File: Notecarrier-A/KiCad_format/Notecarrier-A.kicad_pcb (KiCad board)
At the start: 2 copper layers, 0 parts

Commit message: Establish port of Notecarrier-B PCB.
Ported: components, board outline, fabrication layers, silkscreens and front copper.
To go: inner and back copper layers, drills, sheet metadata.
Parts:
- added ANT1: NN03-310, blues-kicad-lib:ANT-NN03310-LTE_NO-SILK, F.Cu at (79.0, 74.5)
- added ANT2: NN03-320, blues-kicad-lib:ANT-NN03320-GPS_NO-SILK, F.Cu at (59.0, 100.5)
- added BAT1: NU, blues-kicad-lib:BATHLD-2464-NO_MECH, B.Cu at (92.5, 112.8)
- added C1: 47u/16V-X5R, blues-kicad-lib:CS-C-1206, F.Cu at (74.9, 119.5)
- added C10: 100n/16V, blues-kicad-lib:CS-C-0402, F.Cu at (70.7, 116.9)
- added C11: 10n/1kV, blues-kicad-lib:CS-C-1206, F.Cu at (63.1, 119.4)
- added C12: 10u/25V-X5R, blues-kicad-lib:CS-C-1206, F.Cu at (119.0, 129.7)
- added C13: 1u/16V-X5R, blues-kicad-lib:CS-C-0402, F.Cu at (115.5, 116.8)
- added C16: 100n/16V, blues-kicad-lib:CS-C-0402, F.Cu at (110.9, 90.8)
- added C17: 33p/50V-C0G, blues-kicad-lib:CS-C-0402, F.Cu at (113.4, 90.8)
- added C18: 33p/50V-C0G, blues-kicad-lib:CS-C-0402, F.Cu at (111.6, 95.6)
- added C19: 33p/50V-C0G, blues-kicad-lib:CS-C-0402, F.Cu at (113.5, 93.5)
- added C2: 4.7u/6.3V-X5R, blues-kicad-lib:CS-C-0402, F.Cu at (76.5, 120.7)
- added C21: 1n/50V, blues-kicad-lib:FRACTUS-0404_NO-SILK, F.Cu at (57.8, 110.1)
- added C22: 1u/16V-X5R, blues-kicad-lib:CS-C-0402, F.Cu at (64.4, 110.3)
- added C23: 100n/16V, blues-kicad-lib:CS-C-0402, F.Cu at (77.8, 100.1)
- added C25: 0.5p/50V-C0G, blues-kicad-lib:FRACTUS-0404_NO-SILK, F.Cu at (67.2, 78.0)
- added C26: 1p/50V-C0G, blues-kicad-lib:FRACTUS-0404_NO-SILK, F.Cu at (69.4, 89.1)
- added C27: 2.2p/50V-C0G, blues-kicad-lib:FRACTUS-0404_NO-SILK, F.Cu at (67.2, 88.3)
- added C28: 4.6p/50V-C0G, blues-kicad-lib:FRACTUS-0404_NO-SILK, F.Cu at (57.8, 105.8)
- added C29: 1.1p/50V-C0G, blues-kicad-lib:FRACTUS-0404_NO-SILK, F.Cu at (57.0, 103.7)
- added C3: 10u/10V-X5R, blues-kicad-lib:CS-C-0603, F.Cu at (77.9, 118.3)
- added C4: 10u/10V-X5R, blues-kicad-lib:CS-C-0603, F.Cu at (77.9, 117.0)
- added C5: 100n/16V, blues-kicad-lib:CS-C-0402, F.Cu at (80.7, 122.7)
- added C6: 100n/16V, blues-kicad-lib:CS-C-0402, F.Cu at (75.5, 107.2)
- added C7: 10u/6.3V-X5R, blues-kicad-lib:CS-C-0402, F.Cu at (75.5, 108.3)
- added C8: 10u/6.3V-X5R, blues-kicad-lib:CS-C-0402, F.Cu at (74.9, 115.0)
- added C9: 100n/16V, blues-kicad-lib:CS-C-0402, F.Cu at (74.9, 113.9)
- added DS2: FSV1045V, blues-kicad-lib:TO277-3, F.Cu at (75.3, 129.0)
- added DS3: FSV1045V, blues-kicad-lib:TO277-3, F.Cu at (70.2, 129.0)
- added DS4: STPS3H100U, blues-kicad-lib:SMB, F.Cu at (67.1, 123.6)
- added DS5: STPS3H100U, blues-kicad-lib:SMB, F.Cu at (71.4, 123.6)
- added DS6: FSV1045V, blues-kicad-lib:TO277-3, F.Cu at (117.7, 126.0)
- added F1: SF-0603F150-2, blues-kicad-lib:FS-0603, F.Cu at (84.7, 97.5)
- added F2: 3.5A/32V, blues-kicad-lib:FS-0603, F.Cu at (115.2, 101.2)
- added FID1: TPS, blues-kicad-lib:FIDUCIAL, F.Cu at (56.2, 132.7)
- added FID2: TPS, blues-kicad-lib:FIDUCIAL, F.Cu at (128.6, 132.6)
- added FID3: TPS, blues-kicad-lib:FIDUCIAL, B.Cu at (56.2, 132.7)
- added FID4: TPS, blues-kicad-lib:FIDUCIAL, B.Cu at (128.6, 132.6)
- added H1: MountingHole, blues-kicad-lib:FORO-0330-U, F.Cu at (59.5, 76.5)
- added H2: MountingHole, blues-kicad-lib:FORO-0330-U, F.Cu at (125.5, 76.5)
- added H3: MountingHole, blues-kicad-lib:FORO-0330-U, F.Cu at (59.5, 135.5)
- added H4: MountingHole, blues-kicad-lib:FORO-0330-U, F.Cu at (125.5, 135.5)
- added J10: 00711, blues-kicad-lib:J-3-0254-FDT_H0508, F.Cu at (61.4, 93.0)
- added J11: 10118192-0002LF, blues-kicad-lib:J-5-0065-FOS-MICROUSB10118192, F.Cu at (59.7, 126.3)
- added J12: B2B-PH-SM4-TBT(LF)(SN), blues-kicad-lib:J-2-0200-MDS-B2B-PH-SM4, F.Cu at (124.5, 107.0)
- added J13: BM04B-SRSS-TBT, blues-kicad-lib:J-4-0100-MDS-SH_NO-SILK, F.Cu at (119.4, 109.3)
- added J14: BM04B-SRSS-TBT, blues-kicad-lib:J-4-0100-MDS-SH_NO-SILK, F.Cu at (119.4, 104.3)
- added J2: NU, blues-kicad-lib:J-5-0065-FDS-UUSB1051330001_NO-SILK, B.Cu at (62.0, 125.9)
- added J3: B2B-PH-SM4-TBT(LF)(SN), blues-kicad-lib:J-2-0200-MDS-B2B-PH-SM4, F.Cu at (124.5, 128.6)
- added J4: B2B-PH-SM4-TBT(LF)(SN), blues-kicad-lib:J-2-0200-MDS-B2B-PH-SM4, F.Cu at (124.5, 116.8)
- added J5: NanoSIM - SF72S006VBAR2500, blues-kicad-lib:J-NANOSIM-SF72S006VBA_NO-FILL, F.Cu at (122.5, 93.4)
- added J6: MDT420E01001, blues-kicad-lib:J-75-0050-MOS-M2-E, F.Cu at (98.3, 96.3)
- added J7: uFL-R-SMT-1-10, blues-kicad-lib:J-3-MDS-UFL_NO-SILK, F.Cu at (79.8, 89.9)
- added J8: uFL-R-SMT-1-10, blues-kicad-lib:J-3-MDS-UFL_NO-SILK, F.Cu at (67.5, 108.3)
- added J9: 12734, blues-kicad-lib:J-22-0254-FDT-H0508_EDGE, F.Cu at (93.2, 138.7)
- added L1: XFL4020-222MEC, blues-kicad-lib:LS-XFL4020, F.Cu at (78.7, 111.3)
- added L2: 1285AS-H-2R2M=P2, blues-kicad-lib:LS-0806, F.Cu at (80.5, 120.3)
- added L5: LQW15AN7N5H00D, blues-kicad-lib:FRACTUS-0404_NO-SILK, F.Cu at (60.5, 108.7)
- added L6: LQW18AN12NG80, blues-kicad-lib:FRACTUS-0404_NO-SILK, F.Cu at (67.2, 76.7)
- added L7: LQW18AN10NG80D, blues-kicad-lib:FRACTUS-0404_NO-SILK, F.Cu at (71.1, 89.1)
- added L8: LQW18AN8N4G80D, blues-kicad-lib:FRACTUS-0404_NO-SILK, F.Cu at (64.5, 89.1)
- added L9: LQW15AN2N3G80D, blues-kicad-lib:FRACTUS-0404_NO-SILK, F.Cu at (64.5, 86.0)
- added OBJ1: 9774025151R, blues-kicad-lib:DIST-WASMSIM0250, F.Cu at (98.3, 129.6)
- added PAD1: TPS, blues-kicad-lib:PAD-THT-CAS-0100, F.Cu at (130.0, 87.9)
- added PAD2: TPS, blues-kicad-lib:PAD-THT-CAS-0100, F.Cu at (55.0, 87.9)
- added Q1: AO3420, blues-kicad-lib:SOT23, F.Cu at (78.2, 98.5)
- added R1: 10M/5%, blues-kicad-lib:RS-0402, F.Cu at (78.7, 122.7)
- added R10: 10k, blues-kicad-lib:RS-0402, F.Cu at (118.3, 121.5)
- added R12: 22R, blues-kicad-lib:RS-0603, F.Cu at (111.4, 93.1)
- added R14: 22R, blues-kicad-lib:RS-0603, F.Cu at (111.4, 94.4)
- added R15: 22R, blues-kicad-lib:RS-0603, F.Cu at (111.4, 89.6)
- added R16: 15k, blues-kicad-lib:RS-0402, F.Cu at (110.9, 91.9)
- added R18: 200k, blues-kicad-lib:RS-0402, F.Cu at (61.8, 111.0)
- added R21: 1k, blues-kicad-lib:RS-0402, F.Cu at (76.7, 98.1)
- added R22: 100k, blues-kicad-lib:RS-0402, F.Cu at (62.9, 111.0)
- added R25: 0R, blues-kicad-lib:FRACTUS-0404_NO-SILK, F.Cu at (90.8, 76.7)
- added R26: NU, blues-kicad-lib:FRACTUS-0404_NO-SILK, F.Cu at (90.8, 78.0)
- added R27: 0R, blues-kicad-lib:FRACTUS-0404_NO-SILK, F.Cu at (73.3, 88.3)
- added R28: 0R, blues-kicad-lib:FRACTUS-0404_NO-SILK, F.Cu at (76.1, 88.3)
- added R29: 0R, blues-kicad-lib:FRACTUS-0404_NO-SILK, F.Cu at (57.0, 108.0)
- added R30: NU, blues-kicad-lib:RS-0603, F.Cu at (119.9, 102.0)
- added R31: NU, blues-kicad-lib:RS-0603, F.Cu at (119.9, 100.7)
- added R4: 82k, blues-kicad-lib:RS-0402, F.Cu at (73.4, 111.9)
- added R5: 1M, blues-kicad-lib:RS-1206, F.Cu at (60.9, 119.3)
- added R6: 10k, blues-kicad-lib:RS-0402, F.Cu at (118.7, 116.8)
- added R8: 10k, blues-kicad-lib:RS-0402, F.Cu at (117.8, 115.6)
- added R9: 470R, blues-kicad-lib:RS-0402, F.Cu at (118.3, 122.6)
- added RR1: 100R/5%, blues-kicad-lib:RR-8X-1506, F.Cu at (89.9, 134.8)
- added RR2: 100R/5%, blues-kicad-lib:RR-8X-1506, F.Cu at (86.5, 131.4)
- added SW1: CJS-1200TA, blues-kicad-lib:SW_CJS-1200TA_NO-SILK, F.Cu at (79.5, 104.5)
- added TVS1: SM6T6V8A, blues-kicad-lib:SMB, F.Cu at (80.3, 127.0)
- added TVS2: ESDLC5V0M5-TP, blues-kicad-lib:SOT666_NO-SILK, F.Cu at (111.4, 97.5)
- added U1: TPS62748YFPT, blues-kicad-lib:XFBGA8, F.Cu at (78.3, 120.5)
- added U2: MAX17225ELT, blues-kicad-lib:WDFN6-0200X0200, F.Cu at (75.3, 111.4)
- added U3: BQ24210DQCT, blues-kicad-lib:WSON10-EXP_NO-SILK, F.Cu at (117.4, 119.0)
- added U5: BGA725L6E6327FTSA1, blues-kicad-lib:XFDFN6_NO-SILK, F.Cu at (63.1, 108.7)
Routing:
- net (no net): track 0.00 -> 126.7 mm
- net GND: track 0.00 -> 115.5 mm
- net /Connector/TX_P: track 0.00 -> 38.9 mm
- net /Connector/RX_P: track 0.00 -> 38.9 mm
- net /Connector/AUX_RX_P: track 0.00 -> 38.9 mm
- net /Connector/AUX_EN_P: track 0.00 -> 38.9 mm
- net /Connector/AUX_TX_P: track 0.00 -> 38.9 mm
- net /Connector/ATTN_P: track 0.00 -> 38.9 mm
- net /Connector/SCL_P: track 0.00 -> 38.2 mm
- net /Connector/SDA_P: track 0.00 -> 37.9 mm
- net TX: track 0.00 -> 34.1 mm
- net RX: track 0.00 -> 31.5 mm
- net VACT_GPS_OUT: track 0.00 -> 24.8 mm
- net +1V8: track 0.00 -> 24.0 mm
- net /Connector/SIM_NPRESENT: track 0.00 -> 22.1 mm
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- added copper zone on F.Cu, net +1V8
- added copper zone on F.Cu, net +3V3
- added copper zone on F.Cu, net /Connector/GPS_50
- added copper zone on F.Cu, net /Connector/GPS_50_A
- added copper zone on F.Cu, net GND
- added copper zone on F.Cu, net Net-(DS5-K)
- added copper zone on F.Cu, net Net-(J11-Shield)
- added copper zone on F.Cu, net V+
- added copper zone on F.Cu, net VBAT
- added copper zone on F.Cu, net VIO_P
- added copper zone on F.Cu, net VMAIN
- added copper zone on F.Cu, net VMODEM_P
- added copper zone on F.Cu, net VUSB
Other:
- board outline added: 75 x 68 mm
- copper layers 2 -> 4
- board text added: "+"
- board text added: "."
- board text added: "0"
- board text added: "1"
- board text added: "1V8"
- board text added: "2"
- board text added: "2.0"
- board text added: "2017-3047_V16"
- board text added: "3V3"
- board text added: "<BAT"
- board text added: "<MAIN"
- board text added: "<VIO"
- board text added: "<VUSB"
- board text added: "ANT1"
- board text added: "ANT2"
- board text added: "ATTN"
- board text added: "AUX1"
- board text added: "AUX2"
- board text added: "AUX3"
- board text added: "AUX4"
- board text added: "AUXEN"
- board text added: "AUXRX"
- board text added: "AUXTX"
- board text added: "BAT1"
- board text added: "C1"
- board text added: "C10"
- board text added: "C11"
- board text added: "C12"
- board text added: "C13"
- board text added: "C16"
- board text added: "C17"
- board text added: "C18"
- board text added: "C19"
- board text added: "C2"
- board text added: "C21"
- board text added: "C22"
- board text added: "C23"
- board text added: "C25"
- board text added: "C26"
- board text added: "C27"
- board text added: "C28"
- board text added: "C29"
- board text added: "C3"
- board text added: "C4"
- board text added: "C5"
- board text added: "C6"
- board text added: "C7"
- board text added: "C8"
- board text added: "C9"
- board text added: "DS2"
- board text added: "DS3"
- board text added: "DS4"
- board text added: "DS5"
- board text added: "DS6"
- board text added: "EDGE"
- board text added: "EN"
- board text added: "F1"
- board text added: "F2"
- board text added: "FID1"
- board text added: "FID2"
- board text added: "FID3"
- board text added: "FID4"
- board text added: "GND"
- board text added: "GPS"
- board text added: "J10"
- board text added: "J11"
- board text added: "J12"
- board text added: "J13"
- board text added: "J14"
- board text added: "J2"
- board text added: "J3"
- board text added: "J4"
- board text added: "J5"
- board text added: "J6"
- board text added: "J7"
- board text added: "J8"
- board text added: "J9"
- board text added: "L1"
- board text added: "L2"
- board text added: "L5"
- board text added: "L6"
- board text added: "L7"
- board text added: "L8"
- board text added: "L9"
- board text added: "LIPO"
- board text added: "MAIN"
- board text added: "NN"
- board text added: "NOTECARRIER-A"
- board text added: "OBJ1"
- board text added: "Only GND Trace"
- board text added: "PAD1"
- board text added: "PAD2"
- board text added: "Port"
- board text added: "Q1"
- board text added: "QWIIC"
- board text added: "R1"
- board text added: "R10"
- board text added: "R12"
- board text added: "R14"
- board text added: "R15"
- board text added: "R16"
- board text added: "R18"
- board text added: "R21"
- board text added: "R22"
- board text added: "R25"
- board text added: "R26"
- board text added: "R27"
- board text added: "R28"
- board text added: "R29"
- board text added: "R30"
- board text added: "R31"
- board text added: "R4"
- board text added: "R5"
- board text added: "R6"
- board text added: "R8"
- board text added: "R9"
- board text added: "RR1"
- board text added: "RR2"
- board text added: "RST"
- board text added: "RX"
- board text added: "SCL"
- board text added: "SDA"
- board text added: "SOLAR"
- board text added: "SW1"
- board text added: "TVS1"
- board text added: "TVS2"
- board text added: "TX"
- board text added: "U1"
- board text added: "U2"
- board text added: "U3"
- board text added: "U5"
- board text added: "USB Charging"
- board text added: "USB Charging Port"
- board text added: "V+"

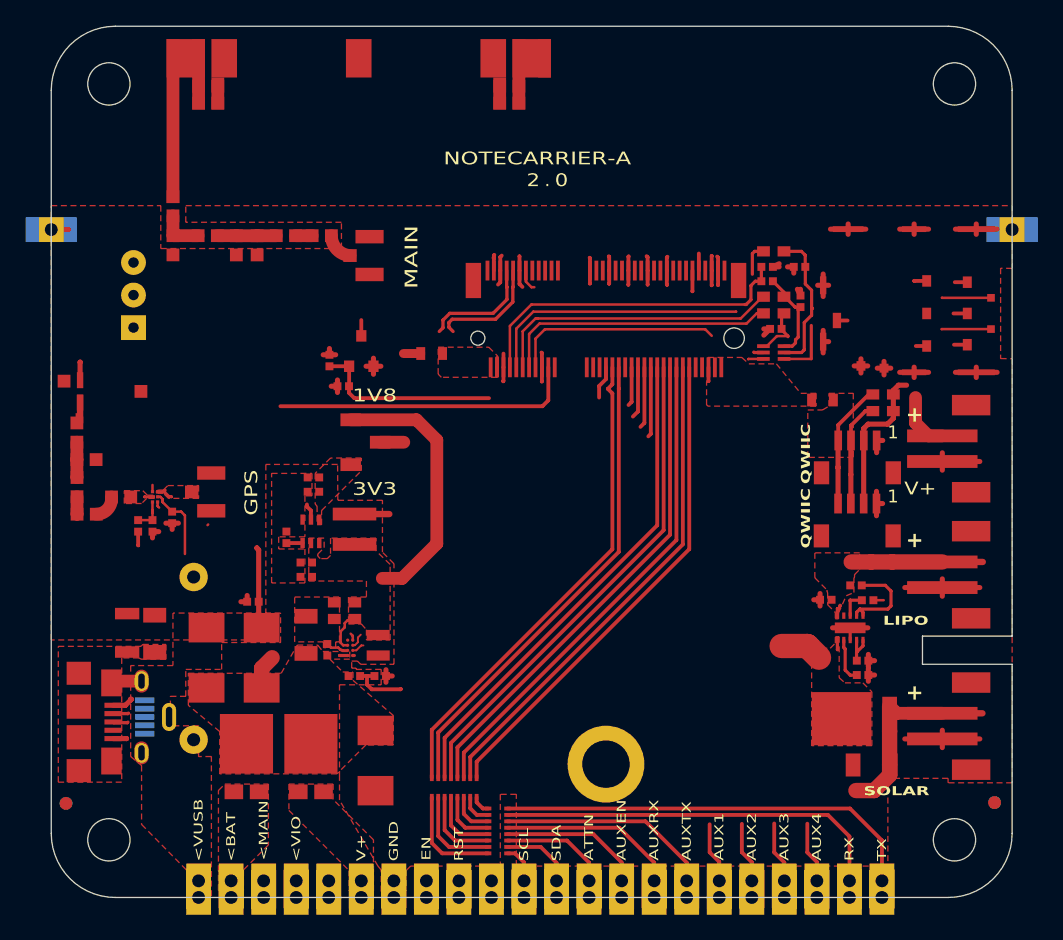
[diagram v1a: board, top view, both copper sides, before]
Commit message: First pass port of Notecarrier-B PCB.
See PortingNotes for details. To go: 3D models and validation.
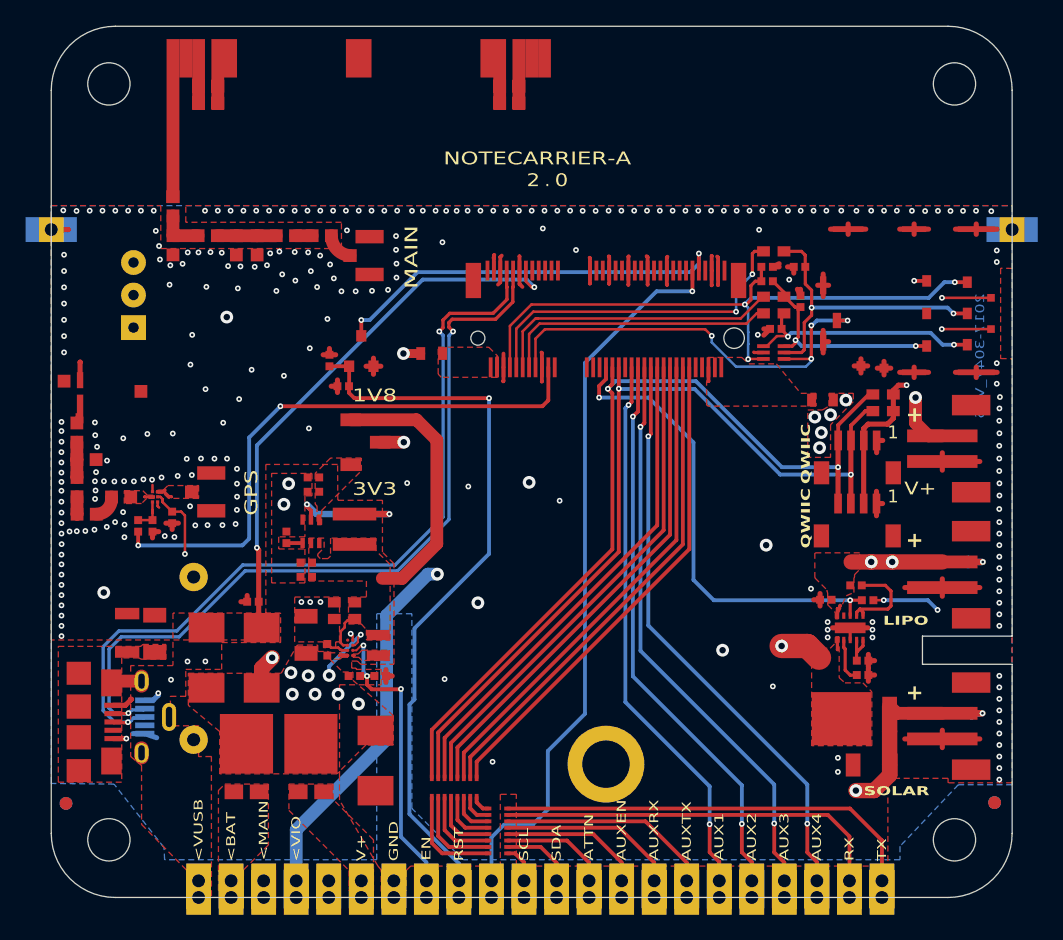
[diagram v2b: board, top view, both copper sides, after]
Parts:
- added TP4: TPS, blues-kicad-lib:TPS-SPEA, B.Cu at (126.6, 113.8)
- added TP5: TPS, blues-kicad-lib:TPS-SPEA, B.Cu at (126.8, 125.6)
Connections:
- C25 pad 1: Net-(ANT1-MN1-A) -> Net-(ANT1-MN1-B)
- C25 pad 2: Net-(ANT1-MN1-B) -> Net-(ANT1-MN1-A)
- R12 pad 1: Net-(J5-I/O) -> /Connector/SIM_IO
- R12 pad 2: /Connector/SIM_IO -> Net-(J5-I/O)
- R14 pad 1: Net-(J5-CLK) -> /Connector/SIM_CLK
- R14 pad 2: /Connector/SIM_CLK -> Net-(J5-CLK)
- R15 pad 1: Net-(J5-RST) -> /Connector/SIM_RST
- R15 pad 2: /Connector/SIM_RST -> Net-(J5-RST)
- R16 pad 1: /Connector/SIM_VCC -> Net-(J5-I/O)
- R16 pad 2: Net-(J5-I/O) -> /Connector/SIM_VCC
- R30 pad 1: VIO -> /Connector/SDA_P
- R30 pad 2: /Connector/SDA_P -> VIO
- R31 pad 1: VIO -> /Connector/SCL_P
- R31 pad 2: /Connector/SCL_P -> VIO
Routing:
- net (no net): track 126.7 -> 0.00 mm
- net V+: track 4.50 -> 82.3 mm, vias 0 -> 1
- net BOOT: track 1.62 -> 57.7 mm, vias 0 -> 1
- net USB_DP: track 10.1 -> 64.2 mm, vias 0 -> 2
- net USB_DM: track 10.2 -> 63.4 mm, vias 0 -> 2
- net /Connector/SIM_VCC: track 2.18 -> 49.7 mm, vias 0 -> 3
- net VSOLAR: track 16.0 -> 63.1 mm, vias 0 -> 2
- net VIO: track 9.88 -> 55.9 mm, vias 0 -> 7
- net RST: track 14.7 -> 57.2 mm, vias 0 -> 1
- net VUSB: track 9.79 -> 46.4 mm, vias 0 -> 6
- net AUX1: track 8.42 -> 44.0 mm, vias 0 -> 2
- net AUX4: track 10.9 -> 46.3 mm, vias 0 -> 2
- net AUX2: track 9.43 -> 44.7 mm, vias 0 -> 2
- net AUX3: track 10.2 -> 45.5 mm, vias 0 -> 2
- net AUX5: track 4.70 -> 37.1 mm, vias 0 -> 2
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- added copper zone on B.Cu, net GND
- added copper zone on In1.Cu, net GND
- added copper zone on In2.Cu, net GND
- added copper zone on In2.Cu, net Net-(DS5-K)
- added copper zone on F.Cu, net Net-(U1-SW)
- added copper zone on In2.Cu, net VBAT
- added copper zone on In2.Cu, net VIO
- added copper zone on In2.Cu, net VMAIN
- added copper zone on In2.Cu, net VUSB
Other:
- board text added: "+/- 10%"
- board text added: "0 mm"
- board text added: "0.02 mm"
- board text added: "0.035 mm"
- board text added: "0.1500 mm / 0.1500 mm"
- board text added: "0.2"
- board text added: "0.2000 mm"
- board text added: "0.26"
- board text added: "0.4 mm"
- board text added: "0.6 mm"
- board text added: "1.5800 mm"
- board text added: "4"
- board text added: "75.0000 mm x 68.0000 mm"
- board text added: "90 ohm"
- board text added: "B.Cu"
- board text added: "B.Mask"
- board text added: "B.Paste"
- board text added: "B.Silkscreen"
- board text added: "BOARD CHARACTERISTICS"
- board text added: "Black"
- board text added: "Board Thickness:"
- board text added: "Board overall dimensions:"
- board text added: "Bottom Silk Screen"
- board text added: "Bottom Solder Mask"
- board text added: "Bottom Solder Paste"
- board text added: "Castellated pads:"
- board text added: "Color"
- board text added: "Copper Finish:"
- board text added: "Copper Layer Count:"
- board text added: "Dielectric"
- board text added: "ENIG"
- board text added: "Edge card connectors:"
- board text added: "F.Cu"
- board text added: "F.Cu and B.Cu thickness layer shown in the table above contains +20um (from IPC-A-600 Class 2) of plating"
- board text added: "F.Mask"
- board text added: "F.Paste"
- board text added: "F.Silkscreen"
- board text added: "FR4-TG150"
- board text added: "IMPEDANCE CONTROL TABLE"
- board text added: "IMPEDANCE DIFFERENTIAL"
- board text added: "IMPEDANCE SINGLE-ENDED"
- board text added: "Impedance Control:"
- board text added: "In1.Cu"
- board text added: "In2.Cu"
- board text added: "LAYER"
- board text added: "Layer Name"
- board text added: "Material"
- board text added: "Min hole diameter:"
- board text added: "Min track/spacing:"
- board text added: "NA"
- board text added: "No"
- board text added: "Not specified"
- board text added: "Plated Board Edge:"
- board text added: "SPACING [MM]"
- board text added: "TOLLERANCE"
- board text added: "TRACE [MM]"
- board text added: "Thickness (mm)"
- board text added: "Top Silk Screen"
- board text added: "Top Solder Mask"
- board text added: "Top Solder Paste"
- board text added: "Type"
- board text added: "White"
- board text added: "Yes"
- board text added: "copper"
- board text added: "core"
- board text added: "prepreg"

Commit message: Release RevA of Notecarrier-A port.
Validation complete. Results in the validation directory, documented in PortingNotes.md.
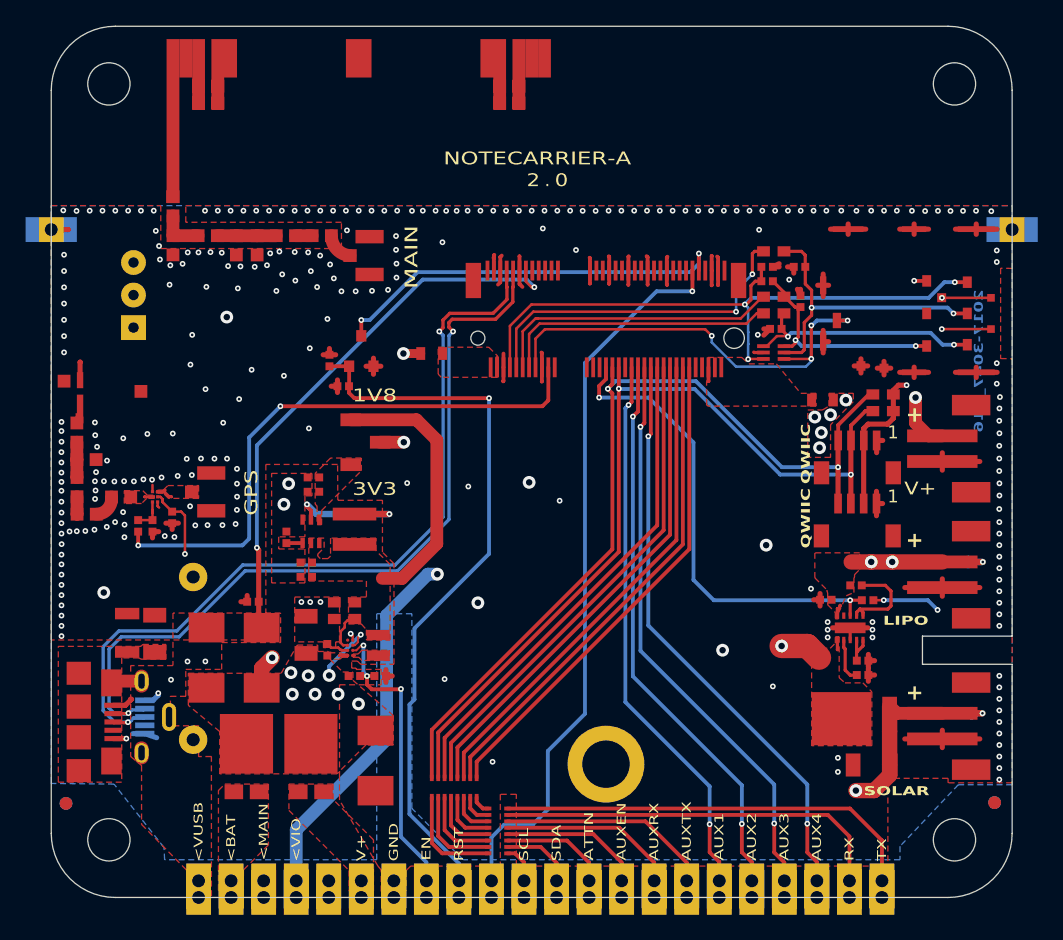
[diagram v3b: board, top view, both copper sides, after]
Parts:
- FID1, FID2, FID3, FID4: footprint blues-kicad-lib:FIDUCIAL -> blues-kicad-lib:FIDUCIAL_MIN-CLEARANCE
- J6: footprint blues-kicad-lib:J-75-0050-MOS-M2-E -> blues-kicad-lib:J-75-0050-MOS-M2-E_smaller-mask
- R6: value 10k -> NU

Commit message: Back port J-5-0065-FOS-USB10118192-NOF footprint from Notecarrier-Pi.
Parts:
- J11: footprint blues-kicad-lib:J-5-0065-FOS-MICROUSB10118192 -> blues-kicad-lib:J-5-0065-FOS-USB10118192-NOF
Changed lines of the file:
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@@
     )
   )
-  (footprint "blues-kicad-lib:J-5-0065-FOS-MICROUSB10118192" (layer "F.Cu")
+  (footprint "blues-kicad-lib:J-5-0065-FOS-USB10118192-NOF" (layer "F.Cu")
     (at 59.7 126.3 -90)
-    (descr "USB Micro-B receptacle, horizontal, SMD, 10118192, https://cdn.amphenol-icc.com/media/wysiwyg/files/drawing/10118192.pdf, ported from OrCAD")
+    (descr "USB Micro-B receptacle, horizontal, SMD, 10118192, https://cdn.amphenol-icc.com/media/wysiwyg/files/drawing/10118192.pdf, no flange, ported from OrCAD")
     (tags "USB Micro B horizontal SMD")
+    (property "Critical" "")
     (property "Description" "CONN. USB F/90° TYPE MICRO-B C.S. 10118192-0002LF FCI SMT")
     (property "Distributor" "FAE")
     (property "MPN" "10118192-0002LF")
+    (property "Manufacturer" "")
     (property "Note" "Full SMD, no FLANGE")
+    (property "Order Code" "")
+    (property "Part Number" "")
     (property "Pkg Type" "SMD")
     (property "Sheetfile" "Notecarrier-A_Power.kicad_sch")
     (property "Sheetname" "Power")
+    (property "Supplier" "")
     (property "Temperature" "-30°..+80°")
     (property "ki_description" "USB Micro Type B connector")
     (property "ki_keywords" "connector USB micro")
     (attr smd)
-    (fp_text reference "J11" (at 0 -2.225 90) (layer "F.SilkS") hide
-        (effects (font (size 1 1) (thickness 0.15)))
-    )
-    (fp_text value "10118192-0002LF" (at 0 6.025 90) (layer "F.Fab") hide
-        (effects (font (size 1 1) (thickness 0.15)))
-    )
-    (fp_text user "${REFERENCE}" (at 0 1.225 90) (layer "F.Fab")
-        (effects (font (size 1 1) (thickness 0.15)))
-    )
-    (fp_text user "EDGE" (at 6.75 3.5 90) (layer "F.Fab")
-        (effects (font (size 1 1) (thickness 0.15)))
-    )
-    (fp_text user "EDGE" (at -6.8 3.5 90) (layer "F.Fab")
+    (fp_text reference "J11" (at 0 -2.225 -90) (layer "F.SilkS") hide
+        (effects (font (size 1 1) (thickness 0.15)))
+    )
+    (fp_text value "10118192-0002LF" (at 0 6.025 -90) (layer "F.Fab") hide
+        (effects (font (size 1 1) (thickness 0.15)))
+    )
+    (fp_text user "EDGE" (at -6.8 3.5 -90) (layer "F.Fab")
+        (effects (font (size 1 1) (thickness 0.15)))
+    )
+    (fp_text user "${REFERENCE}" (at 0 1.225 -90) (layer "F.Fab")
+        (effects (font (size 1 1) (thickness 0.15)))
+    )
+    (fp_text user "EDGE" (at 6.75 3.5 -90) (layer "F.Fab")
         (effects (font (size 1 1) (thickness 0.15)))
     )
@@
     (pad "6" smd rect (at 3.8 2.55 270) (size 1.8 1.9) (layers "F.Cu" "F.Paste" "F.Mask")
       (net 113 "Net-(#PWR037-USB_SHIELD)") (pinfunction "Shield") (pintype "passive") (solder_mask_margin 0.05))
-    (model "${BLUES_KICAD_LIB_DIR}/3d-models/J-5-0065-FOS-MICROUSB10118192.step"
-      (offset (xyz 0 0 0))
-      (scale (xyz 1 1 1))
-      (rotate (xyz 0 0 0))
-    )
-    (model "${BLUES_KICAD_LIB_DIR}/3d-models/J-5-0065-FOS-USB10118192-NOF.step" hide
+    (model "${BLUES_KICAD_LIB_DIR}/3d-models/J-5-0065-FOS-USB10118192-NOF.step"
       (offset (xyz 0 0 0))
       (scale (xyz 1 1 1))
@@
     (property "ki_keywords" "test point tp")
     (clearance 0.2)
-    (attr exclude_from_pos_files exclude_from_bom)
+    (attr exclude_from_pos_files)
     (fp_text reference "TP5" (at 0 1.448) (layer "B.SilkS") hide
         (effects (font (size 1 1) (thickness 0.15)) (justify mirror))
@@
     (property "ki_keywords" "test point tp")
     (clearance 0.2)
-    (attr exclude_from_pos_files exclude_from_bom)
+    (attr exclude_from_pos_files)
     (fp_text reference "TP4" (at 0 1.448) (layer "B.SilkS") hide
         (effects (font (size 1 1) (thickness 0.15)) (justify mirror))
